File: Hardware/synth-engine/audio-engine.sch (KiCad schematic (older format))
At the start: 23 parts

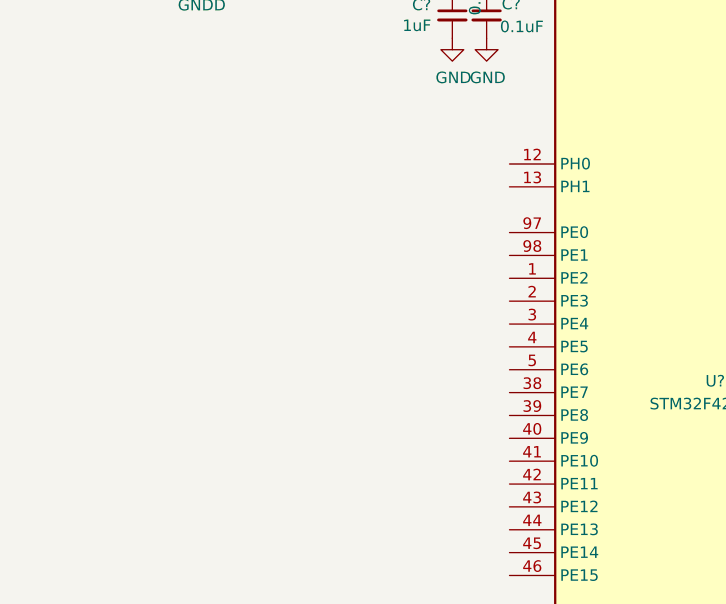
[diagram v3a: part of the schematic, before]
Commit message: add (optional) external crystal to STM32 schematic. I don't know if an external crystal is necessary or not but it's good to have pads for it on the board if I need it. As I understand it, timing critical comms protocols might need the improved accuracy of an external crystal. So, I think I2S is the only thing that might qualify in this application, because the PSoC is handling USB. Otherwise, the internal oscillator might be fine.
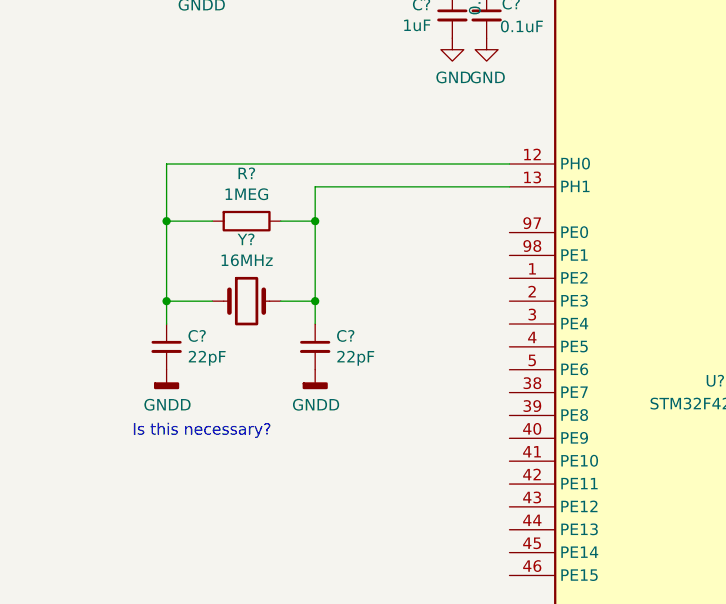
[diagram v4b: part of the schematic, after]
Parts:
- added C? (x2): 22pF, symbol Device:C_Small
- added R?: 1MEG, symbol Device:R
- added Y?: 16MHz, symbol Device:Crystal
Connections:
- net GNDD: now also C?.2, C?.2
- net at U?.12 (PH0): now also C?.1, R?.2, Y?.1
- net at U?.13 (PH1): now also C?.1, R?.1, Y?.2
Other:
- note added: "Is this necessary?"
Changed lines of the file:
@@
 Text Label 4600 3700 0    50   ~ 0
 NRST
+$Comp
+L Device:R R?
+U 1 1 5DDE8ED5
+P 1650 3250
+F 0 "R?" V 1443 3250 50  0000 C CNN
+F 1 "1MEG" V 1534 3250 50  0000 C CNN
+F 2 "" V 1580 3250 50  0001 C CNN
+F 3 "~" H 1650 3250 50  0001 C CNN
+	1    1650 3250
+	0    1    1    0
+$EndComp
+$Comp
+L Device:C_Small C?
+U 1 1 5DDE8EDC
+P 1300 3800
+F 0 "C?" H 1392 3846 50  0000 L CNN
+F 1 "22pF" H 1392 3755 50  0000 L CNN
+F 2 "" H 1300 3800 50  0001 C CNN
+F 3 "~" H 1300 3800 50  0001 C CNN
+	1    1300 3800
+	1    0    0    -1
+$EndComp
+$Comp
+L Device:C_Small C?
+U 1 1 5DDE8EE3
+P 1950 3800
+F 0 "C?" H 2042 3846 50  0000 L CNN
+F 1 "22pF" H 2042 3755 50  0000 L CNN
+F 2 "" H 1950 3800 50  0001 C CNN
+F 3 "~" H 1950 3800 50  0001 C CNN
+	1    1950 3800
+	1    0    0    -1
+$EndComp
+$Comp
+L Device:Crystal Y?
+U 1 1 5DDE8EEA
+P 1650 3600
+AR Path="/5DDBDEEA/5DDE8EEA" Ref="Y?"  Part="1"
+AR Path="/5DDC7BB6/5DDE8EEA" Ref="Y?"  Part="1"
+F 0 "Y?" H 1650 3868 50  0000 C CNN
+F 1 "16MHz" H 1650 3777 50  0000 C CNN
+F 2 "" H 1650 3600 50  0001 C CNN
+F 3 "~" H 1650 3600 50  0001 C CNN
+	1    1650 3600
+	1    0    0    -1
+$EndComp
+Wire Wire Line
+	1950 3700 1950 3600
+Wire Wire Line
+	1950 3250 1800 3250
+Wire Wire Line
+	1800 3600 1950 3600
+Connection ~ 1950 3600
+Wire Wire Line
+	1950 3600 1950 3250
+Wire Wire Line
+	1500 3250 1300 3250
+Wire Wire Line
+	1300 3250 1300 3600
+$Comp
+L power:GNDD #PWR?
+U 1 1 5DDE8EF8
+P 1300 3900
+F 0 "#PWR?" H 1300 3650 50  0001 C CNN
+F 1 "GNDD" H 1304 3745 50  0000 C CNN
+F 2 "" H 1300 3900 50  0001 C CNN
+F 3 "" H 1300 3900 50  0001 C CNN
+	1    1300 3900
+	1    0    0    -1
+$EndComp
+$Comp
+L power:GNDD #PWR?
+U 1 1 5DDE8EFE
+P 1950 3900
+F 0 "#PWR?" H 1950 3650 50  0001 C CNN
+F 1 "GNDD" H 1954 3745 50  0000 C CNN
+F 2 "" H 1950 3900 50  0001 C CNN
+F 3 "" H 1950 3900 50  0001 C CNN
+	1    1950 3900
+	1    0    0    -1
+$EndComp
+Wire Wire Line
+	1500 3600 1300 3600
+Connection ~ 1300 3600
+Wire Wire Line
+	1300 3600 1300 3700
+Wire Wire Line
+	1950 3100 1950 3250
+Connection ~ 1950 3250
+Connection ~ 1300 3250
+Text Notes 1150 4200 0    50   ~ 0
+Is this necessary?
+Wire Wire Line
+	2800 3100 1950 3100
+Wire Wire Line
+	2800 3000 1300 3000
+Wire Wire Line
+	1300 3000 1300 3250
 $EndSCHEMATC

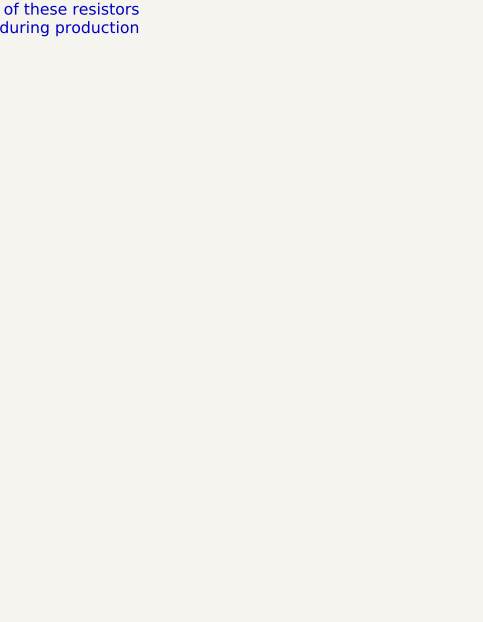
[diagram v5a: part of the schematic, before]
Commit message: add I/O connections between DAC and STM32 pages
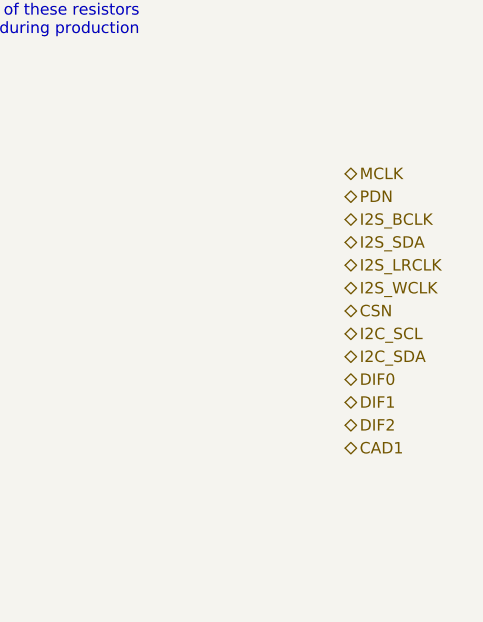
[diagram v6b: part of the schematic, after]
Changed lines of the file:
@@
 Wire Wire Line
 	1300 3000 1300 3250
+Text HLabel 6850 4300 2    50   BiDi ~ 0
+PDN
+Text HLabel 6850 4400 2    50   BiDi ~ 0
+I2S_BCLK
+Text HLabel 6850 4500 2    50   BiDi ~ 0
+I2S_SDA
+Text HLabel 6850 4600 2    50   BiDi ~ 0
+I2S_LRCLK
+Text HLabel 6850 4700 2    50   BiDi ~ 0
+I2S_WCLK
+Text HLabel 6850 4800 2    50   BiDi ~ 0
+CSN
+Text HLabel 6850 4900 2    50   BiDi ~ 0
+I2C_SCL
+Text HLabel 6850 5000 2    50   BiDi ~ 0
+I2C_SDA
+Text HLabel 6850 5100 2    50   BiDi ~ 0
+DIF0
+Text HLabel 6850 5200 2    50   BiDi ~ 0
+DIF1
+Text HLabel 6850 5300 2    50   BiDi ~ 0
+DIF2
+Text HLabel 6850 4200 2    50   BiDi ~ 0
+MCLK
+Text HLabel 6850 5400 2    50   BiDi ~ 0
+CAD1
 $EndSCHEMATC

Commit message: add filtering in front of 3.3V regulators
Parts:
- removed FB?: Ferrite_Bead, symbol Device:Ferrite_Bead
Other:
- moved on the sheet: C?, R?, Y?
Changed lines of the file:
@@
 $EndComp
-$Comp
-L power:+3.3VA #PWR?
-U 1 1 5DDA7288
-P 1900 950
-F 0 "#PWR?" H 1900 800 50  0001 C CNN
-F 1 "+3.3VA" H 1915 1123 50  0000 C CNN
-F 2 "" H 1900 950 50  0001 C CNN
-F 3 "" H 1900 950 50  0001 C CNN
-	1    1900 950
-	1    0    0    -1
-$EndComp
-$Comp
-L SparkFun-Aesthetics:3.3V #SUPPLY?
-U 1 1 5DDA72B4
-P 1150 950
-F 0 "#SUPPLY?" H 1150 950 50  0001 L BNN
-F 1 "3.3V" H 1150 1124 50  0000 C CNN
-F 2 "" H 1150 950 50  0001 C CNN
-F 3 "" H 1150 950 50  0001 C CNN
-	1    1150 950
-	1    0    0    -1
-$EndComp
-$Comp
-L Device:Ferrite_Bead FB?
-U 1 1 5DDA73A6
-P 1500 950
-F 0 "FB?" V 1226 950 50  0000 C CNN
-F 1 "Ferrite_Bead" V 1317 950 50  0000 C CNN
-F 2 "" V 1430 950 50  0001 C CNN
-F 3 "~" H 1500 950 50  0001 C CNN
-	1    1500 950
-	0    1    1    0
-$EndComp
-Wire Wire Line
-	1150 950  1350 950
-Wire Wire Line
-	1900 950  1650 950
 $Comp
 L Device:R R?
@@
 L Device:R R?
 U 1 1 5DDE8ED5
-P 1650 3250
-F 0 "R?" V 1443 3250 50  0000 C CNN
-F 1 "1MEG" V 1534 3250 50  0000 C CNN
-F 2 "" V 1580 3250 50  0001 C CNN
-F 3 "~" H 1650 3250 50  0001 C CNN
-	1    1650 3250
+P 2050 3250
+F 0 "R?" V 1843 3250 50  0000 C CNN
+F 1 "1MEG" V 1934 3250 50  0000 C CNN
+F 2 "" V 1980 3250 50  0001 C CNN
+F 3 "~" H 2050 3250 50  0001 C CNN
+	1    2050 3250
 	0    1    1    0
 $EndComp
@@
 L Device:C_Small C?
 U 1 1 5DDE8EDC
-P 1300 3800
-F 0 "C?" H 1392 3846 50  0000 L CNN
-F 1 "22pF" H 1392 3755 50  0000 L CNN
-F 2 "" H 1300 3800 50  0001 C CNN
-F 3 "~" H 1300 3800 50  0001 C CNN
-	1    1300 3800
+P 1700 3800
+F 0 "C?" H 1792 3846 50  0000 L CNN
+F 1 "22pF" H 1792 3755 50  0000 L CNN
+F 2 "" H 1700 3800 50  0001 C CNN
+F 3 "~" H 1700 3800 50  0001 C CNN
+	1    1700 3800
 	1    0    0    -1
 $EndComp
@@
 L Device:C_Small C?
 U 1 1 5DDE8EE3
-P 1950 3800
-F 0 "C?" H 2042 3846 50  0000 L CNN
-F 1 "22pF" H 2042 3755 50  0000 L CNN
-F 2 "" H 1950 3800 50  0001 C CNN
-F 3 "~" H 1950 3800 50  0001 C CNN
-	1    1950 3800
+P 2350 3800
+F 0 "C?" H 2442 3846 50  0000 L CNN
+F 1 "22pF" H 2442 3755 50  0000 L CNN
+F 2 "" H 2350 3800 50  0001 C CNN
+F 3 "~" H 2350 3800 50  0001 C CNN
+	1    2350 3800
 	1    0    0    -1
 $EndComp
@@
 L Device:Crystal Y?
 U 1 1 5DDE8EEA
-P 1650 3600
+P 2050 3600
 AR Path="/5DDBDEEA/5DDE8EEA" Ref="Y?"  Part="1"
 AR Path="/5DDC7BB6/5DDE8EEA" Ref="Y?"  Part="1"
-F 0 "Y?" H 1650 3868 50  0000 C CNN
-F 1 "16MHz" H 1650 3777 50  0000 C CNN
-F 2 "" H 1650 3600 50  0001 C CNN
-F 3 "~" H 1650 3600 50  0001 C CNN
-	1    1650 3600
-	1    0    0    -1
-$EndComp
-Wire Wire Line
-	1950 3700 1950 3600
-Wire Wire Line
-	1950 3250 1800 3250
-Wire Wire Line
-	1800 3600 1950 3600
-Connection ~ 1950 3600
-Wire Wire Line
-	1950 3600 1950 3250
-Wire Wire Line
-	1500 3250 1300 3250
-Wire Wire Line
-	1300 3250 1300 3600
+F 0 "Y?" H 2050 3868 50  0000 C CNN
+F 1 "16MHz" H 2050 3777 50  0000 C CNN
+F 2 "" H 2050 3600 50  0001 C CNN
+F 3 "~" H 2050 3600 50  0001 C CNN
+	1    2050 3600
+	1    0    0    -1
+$EndComp
+Wire Wire Line
+	2350 3700 2350 3600
+Wire Wire Line
+	2350 3250 2200 3250
+Wire Wire Line
+	2200 3600 2350 3600
+Connection ~ 2350 3600
+Wire Wire Line
+	2350 3600 2350 3250
+Wire Wire Line
+	1900 3250 1700 3250
+Wire Wire Line
+	1700 3250 1700 3600
 $Comp
 L power:GNDD #PWR?
 U 1 1 5DDE8EF8
-P 1300 3900
-F 0 "#PWR?" H 1300 3650 50  0001 C CNN
-F 1 "GNDD" H 1304 3745 50  0000 C CNN
-F 2 "" H 1300 3900 50  0001 C CNN
-F 3 "" H 1300 3900 50  0001 C CNN
-	1    1300 3900
+P 1700 3900
+F 0 "#PWR?" H 1700 3650 50  0001 C CNN
+F 1 "GNDD" H 1704 3745 50  0000 C CNN
+F 2 "" H 1700 3900 50  0001 C CNN
+F 3 "" H 1700 3900 50  0001 C CNN
+	1    1700 3900
 	1    0    0    -1
 $EndComp
@@
 L power:GNDD #PWR?
 U 1 1 5DDE8EFE
-P 1950 3900
-F 0 "#PWR?" H 1950 3650 50  0001 C CNN
-F 1 "GNDD" H 1954 3745 50  0000 C CNN
-F 2 "" H 1950 3900 50  0001 C CNN
-F 3 "" H 1950 3900 50  0001 C CNN
-	1    1950 3900
-	1    0    0    -1
-$EndComp
-Wire Wire Line
-	1500 3600 1300 3600
-Connection ~ 1300 3600
-Wire Wire Line
-	1300 3600 1300 3700
-Wire Wire Line
-	1950 3100 1950 3250
-Connection ~ 1950 3250
-Connection ~ 1300 3250
+P 2350 3900
+F 0 "#PWR?" H 2350 3650 50  0001 C CNN
+F 1 "GNDD" H 2354 3745 50  0000 C CNN
+F 2 "" H 2350 3900 50  0001 C CNN
+F 3 "" H 2350 3900 50  0001 C CNN
+	1    2350 3900
+	1    0    0    -1
+$EndComp
+Wire Wire Line
+	1900 3600 1700 3600
+Connection ~ 1700 3600
+Wire Wire Line
+	1700 3600 1700 3700
+Wire Wire Line
+	2350 3100 2350 3250
+Connection ~ 2350 3250
+Connection ~ 1700 3250
 Text Notes 1150 4200 0    50   ~ 0
 Is this necessary?
 Wire Wire Line
-	2800 3100 1950 3100
-Wire Wire Line
-	2800 3000 1300 3000
-Wire Wire Line
-	1300 3000 1300 3250
+	2800 3100 2350 3100
+Wire Wire Line
+	2800 3000 1700 3000
+Wire Wire Line
+	1700 3000 1700 3250
 Text HLabel 6850 4300 2    50   BiDi ~ 0
 PDN

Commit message: add I2S, I2C, UART, DAC config pins to STM32
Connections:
- net CAD1: now also U?.43 (PE12)
- net CSN: now also U?.39 (PE8)
- net DIF0: now also U?.40 (PE9)
- net DIF1: now also U?.41 (PE10)
- net DIF2: now also U?.42 (PE11)
- net I2C_SCL: now also U?.92 (PB6)
- net I2C_SDA: now also U?.93 (PB7)
- net I2S_BCLK: now also U?.47 (PB10)
- net I2S_LRCLK: now also U?.51 (PB12)
- net I2S_SDA: now also U?.18 (PC3)
- net MCLK: now also U?.63 (PC6)
- net PDN: now also U?.38 (PE7)
- net UART_TX: now reaches U?.23 (PA0)
- net UART_RX: now reaches U?.24 (PA1)
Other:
- moved on the sheet: C?, R?
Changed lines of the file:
@@
 L Device:C_Small C?
 U 1 1 5DD939E7
-P 5000 1500
-F 0 "C?" H 4850 1550 50  0000 L CNN
-F 1 "0.1uF" H 4750 1450 50  0000 L CNN
-F 2 "" H 5000 1500 50  0001 C CNN
-F 3 "~" H 5000 1500 50  0001 C CNN
-	1    5000 1500
+P 5400 1500
+F 0 "C?" H 5250 1550 50  0000 L CNN
+F 1 "0.1uF" H 5150 1450 50  0000 L CNN
+F 2 "" H 5400 1500 50  0001 C CNN
+F 3 "~" H 5400 1500 50  0001 C CNN
+	1    5400 1500
 	1    0    0    -1
 $EndComp
@@
 L Device:C_Small C?
 U 1 1 5DD93A1D
-P 5150 1500
-F 0 "C?" H 5242 1546 50  0000 L CNN
-F 1 "1uF" H 5242 1455 50  0000 L CNN
-F 2 "" H 5150 1500 50  0001 C CNN
-F 3 "~" H 5150 1500 50  0001 C CNN
-	1    5150 1500
+P 5550 1500
+F 0 "C?" H 5642 1546 50  0000 L CNN
+F 1 "1uF" H 5642 1455 50  0000 L CNN
+F 2 "" H 5550 1500 50  0001 C CNN
+F 3 "~" H 5550 1500 50  0001 C CNN
+	1    5550 1500
 	1    0    0    -1
 $EndComp
@@
 L power:GND #PWR?
 U 1 1 5DD94B9B
-P 5150 1600
-F 0 "#PWR?" H 5150 1350 50  0001 C CNN
-F 1 "GND" H 5155 1427 50  0000 C CNN
-F 2 "" H 5150 1600 50  0001 C CNN
-F 3 "" H 5150 1600 50  0001 C CNN
-	1    5150 1600
+P 5550 1600
+F 0 "#PWR?" H 5550 1350 50  0001 C CNN
+F 1 "GND" H 5555 1427 50  0000 C CNN
+F 2 "" H 5550 1600 50  0001 C CNN
+F 3 "" H 5550 1600 50  0001 C CNN
+	1    5550 1600
 	1    0    0    -1
 $EndComp
@@
 L power:GND #PWR?
 U 1 1 5DD971D0
-P 5000 1600
-F 0 "#PWR?" H 5000 1350 50  0001 C CNN
-F 1 "GND" H 5005 1427 50  0000 C CNN
-F 2 "" H 5000 1600 50  0001 C CNN
-F 3 "" H 5000 1600 50  0001 C CNN
-	1    5000 1600
+P 5400 1600
+F 0 "#PWR?" H 5400 1350 50  0001 C CNN
+F 1 "GND" H 5405 1427 50  0000 C CNN
+F 2 "" H 5400 1600 50  0001 C CNN
+F 3 "" H 5400 1600 50  0001 C CNN
+	1    5400 1600
 	1    0    0    -1
 $EndComp
@@
 	3150 1250 3400 1250
 Wire Wire Line
-	5150 1250 5150 1400
-Wire Wire Line
-	4100 1250 5000 1250
-Wire Wire Line
-	5000 1250 5000 1400
-Connection ~ 5000 1250
-Wire Wire Line
-	5000 1250 5100 1250
+	5550 1250 5550 1400
+Wire Wire Line
+	4100 1250 5400 1250
+Wire Wire Line
+	5400 1250 5400 1400
+Connection ~ 5400 1250
+Wire Wire Line
+	5400 1250 5500 1250
 $Comp
 L power:+3.3VA #PWR?
@@
 L power:+3.3VA #PWR?
 U 1 1 5DDB5916
-P 5100 1150
-F 0 "#PWR?" H 5100 1000 50  0001 C CNN
-F 1 "+3.3VA" H 5115 1323 50  0000 C CNN
-F 2 "" H 5100 1150 50  0001 C CNN
-F 3 "" H 5100 1150 50  0001 C CNN
-	1    5100 1150
-	1    0    0    -1
-$EndComp
-Wire Wire Line
-	5100 1150 5100 1250
-Connection ~ 5100 1250
-Wire Wire Line
-	5100 1250 5150 1250
+P 5500 1150
+F 0 "#PWR?" H 5500 1000 50  0001 C CNN
+F 1 "+3.3VA" H 5515 1323 50  0000 C CNN
+F 2 "" H 5500 1150 50  0001 C CNN
+F 3 "" H 5500 1150 50  0001 C CNN
+	1    5500 1150
+	1    0    0    -1
+$EndComp
+Wire Wire Line
+	5500 1150 5500 1250
+Connection ~ 5500 1250
+Wire Wire Line
+	5500 1250 5550 1250
 $Comp
 L SparkFun-Aesthetics:3.3V #SUPPLY?
@@
 L SparkFun-Aesthetics:3.3V #SUPPLY?
 U 1 1 5DDC2F64
-P 5000 3150
-F 0 "#SUPPLY?" H 5000 3150 50  0001 L BNN
-F 1 "3.3V" H 5000 3324 50  0000 C CNN
-F 2 "" H 5000 3150 50  0001 C CNN
-F 3 "" H 5000 3150 50  0001 C CNN
-	1    5000 3150
+P 5150 3150
+F 0 "#SUPPLY?" H 5150 3150 50  0001 L BNN
+F 1 "3.3V" H 5150 3324 50  0000 C CNN
+F 2 "" H 5150 3150 50  0001 C CNN
+F 3 "" H 5150 3150 50  0001 C CNN
+	1    5150 3150
 	-1   0    0    -1
 $EndComp
@@
 L power:GNDD #PWR?
 U 1 1 5DDC2F6A
-P 5000 3850
-F 0 "#PWR?" H 5000 3600 50  0001 C CNN
-F 1 "GNDD" H 5004 3695 50  0000 C CNN
-F 2 "" H 5000 3850 50  0001 C CNN
-F 3 "" H 5000 3850 50  0001 C CNN
-	1    5000 3850
+P 5150 3850
+F 0 "#PWR?" H 5150 3600 50  0001 C CNN
+F 1 "GNDD" H 5154 3695 50  0000 C CNN
+F 2 "" H 5150 3850 50  0001 C CNN
+F 3 "" H 5150 3850 50  0001 C CNN
+	1    5150 3850
 	-1   0    0    -1
 $EndComp
@@
 L Device:R R?
 U 1 1 5DDC2F70
-P 5000 3300
-F 0 "R?" H 4930 3254 50  0000 R CNN
-F 1 "10k" H 4930 3345 50  0000 R CNN
-F 2 "" V 4930 3300 50  0001 C CNN
-F 3 "~" H 5000 3300 50  0001 C CNN
-	1    5000 3300
+P 5150 3300
+F 0 "R?" H 5080 3254 50  0000 R CNN
+F 1 "10k" H 5080 3345 50  0000 R CNN
+F 2 "" V 5080 3300 50  0001 C CNN
+F 3 "~" H 5150 3300 50  0001 C CNN
+	1    5150 3300
 	-1   0    0    1
 $EndComp
@@
 L Device:R R?
 U 1 1 5DDC2F76
-P 5000 3700
-F 0 "R?" H 4930 3654 50  0000 R CNN
-F 1 "10k" H 4930 3745 50  0000 R CNN
-F 2 "" V 4930 3700 50  0001 C CNN
-F 3 "~" H 5000 3700 50  0001 C CNN
-	1    5000 3700
+P 5150 3700
+F 0 "R?" H 5080 3654 50  0000 R CNN
+F 1 "10k" H 5080 3745 50  0000 R CNN
+F 2 "" V 5080 3700 50  0001 C CNN
+F 3 "~" H 5150 3700 50  0001 C CNN
+	1    5150 3700
 	-1   0    0    1
 $EndComp
@@
 only populate one\nof these resistors\nduring production
 Wire Wire Line
-	5000 3450 5000 3500
-Connection ~ 5000 3500
-Wire Wire Line
-	5000 3500 5000 3550
+	5150 3450 5150 3500
+Connection ~ 5150 3500
+Wire Wire Line
+	5150 3500 5150 3550
 $Comp
 L Connector_Generic:Conn_01x06 J?
@@
 SWO
 Wire Wire Line
-	4600 3500 5000 3500
+	4600 3500 5150 3500
 Text Label 2800 1600 2    50   ~ 0
 NRST
@@
 Wire Wire Line
 	1700 3000 1700 3250
-Text HLabel 6850 4300 2    50   BiDi ~ 0
+Text HLabel 2800 4000 0    50   BiDi ~ 0
 PDN
-Text HLabel 6850 4400 2    50   BiDi ~ 0
+Text HLabel 4600 4300 2    50   BiDi ~ 0
 I2S_BCLK
-Text HLabel 6850 4500 2    50   BiDi ~ 0
+Text HLabel 4600 5300 2    50   BiDi ~ 0
 I2S_SDA
-Text HLabel 6850 4600 2    50   BiDi ~ 0
+Text HLabel 4600 4500 2    50   BiDi ~ 0
 I2S_LRCLK
-Text HLabel 6850 4700 2    50   BiDi ~ 0
+Text HLabel 5200 4500 2    50   BiDi ~ 0
 I2S_WCLK
-Text HLabel 6850 4800 2    50   BiDi ~ 0
+Text HLabel 2800 4100 0    50   BiDi ~ 0
 CSN
-Text HLabel 6850 4900 2    50   BiDi ~ 0
+Text HLabel 4600 3900 2    50   BiDi ~ 0
 I2C_SCL
-Text HLabel 6850 5000 2    50   BiDi ~ 0
+Text HLabel 4600 4000 2    50   BiDi ~ 0
 I2C_SDA
-Text HLabel 6850 5100 2    50   BiDi ~ 0
+Text HLabel 2800 4200 0    50   BiDi ~ 0
 DIF0
-Text HLabel 6850 5200 2    50   BiDi ~ 0
+Text HLabel 2800 4300 0    50   BiDi ~ 0
 DIF1
-Text HLabel 6850 5300 2    50   BiDi ~ 0
+Text HLabel 2800 4400 0    50   BiDi ~ 0
 DIF2
-Text HLabel 6850 4200 2    50   BiDi ~ 0
+Text HLabel 4600 5600 2    50   BiDi ~ 0
 MCLK
-Text HLabel 6850 5400 2    50   BiDi ~ 0
+Text HLabel 2800 4500 0    50   BiDi ~ 0
 CAD1
+Text HLabel 4600 1600 2    50   Input ~ 0
+UART_TX
+Text HLabel 4600 1700 2    50   Input ~ 0
+UART_RX
 $EndSCHEMATC
